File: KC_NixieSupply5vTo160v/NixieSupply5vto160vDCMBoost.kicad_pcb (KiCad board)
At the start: 2 copper layers, 38.2 x 37.9 mm, 45 parts, among them J1 Screw_Terminal_01x04, J2 CONN_01X01, J3 CONN_01X01, J4 CONN_01X01, J5 CONN_01X01, P1 USB_OTG, Q1 FDS2672CT, Q26 MMBT42, U1 UCC3803

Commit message: Updated the copyright information to Mark Smith and added www.surfncircuits.com to Boards Also added a part number and date code.    yyww (last two digits of year and ww is the work week) NixieSupply Rev2_1804 NixieSupplyMini Rev1_1804
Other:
- board text added: "Mark Smith"
- board text added: "NixieSupply Rev2_1804"
- board text added: "copyright (c) 2018"
- board text added: "www.surfncircuits.com"
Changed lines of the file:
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@@
-(kicad_pcb (version 4) (host pcbnew 4.0.7-e2-6376~58~ubuntu14.04.1)
+(kicad_pcb (version 4) (host pcbnew 4.0.7-e2-6376~60~ubuntu17.10.1)
   (general
     (links 84)
@@
     (area 17.081499 66.616595 229.894856 177.128)
     (thickness 1.6)
-    (drawings 10)
+    (drawings 14)
     (tracks 383)
     (zones 0)
@@
   (page A4)
   (layers
-    (0 F.Cu signal)
-    (31 B.Cu signal)
-    (34 B.Paste user)
-    (35 F.Paste user)
+    (0 F.Cu signal hide)
+    (31 B.Cu signal hide)
+    (34 B.Paste user hide)
+    (35 F.Paste user hide)
     (36 B.SilkS user)
-    (37 F.SilkS user)
-    (38 B.Mask user)
-    (39 F.Mask user)
-    (41 Cmts.User user)
+    (37 F.SilkS user hide)
+    (38 B.Mask user hide)
+    (39 F.Mask user hide)
+    (41 Cmts.User user hide)
     (44 Edge.Cuts user)
-    (45 Margin user)
-    (46 B.CrtYd user)
-    (47 F.CrtYd user)
-    (48 B.Fab user)
-    (49 F.Fab user)
+    (45 Margin user hide)
+    (46 B.CrtYd user hide)
+    (47 F.CrtYd user hide)
+    (48 B.Fab user hide)
+    (49 F.Fab user hide)
   )
   (setup
@@
     )
   )
+  (gr_text www.surfncircuits.com (at 152.654 105.2195) (layer B.SilkS)
+    (effects (font (size 1.5 1.5) (thickness 0.3)) (justify mirror))
+  )
+  (gr_text "copyright (c) 2018" (at 154.8765 107.569) (layer B.SilkS)
+    (effects (font (size 1.5 1.5) (thickness 0.3)) (justify mirror))
+  )
+  (gr_text "NixieSupply  Rev2_1804" (at 155.2575 98.679) (layer B.SilkS)
+    (effects (font (size 1.5 1.5) (thickness 0.3)) (justify mirror))
+  )
+  (gr_text "Mark Smith" (at 155.575 109.601) (layer B.SilkS)
+    (effects (font (size 1.5 1.5) (thickness 0.3)) (justify mirror))
+  )
   (dimension 37.858719 (width 0.3) (layer F.Fab)

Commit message: Added OSHW_LOGO and the copyright symbol to both Files.    Also updated the gerber files and finished the Mini layout solution.
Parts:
- added G***: OSHW_logo_silkscreen-front_5mm, OSHW_logo_silkscreen-front_5mm, B.Cu at (155.8, 102.2)
- added G***: LOGO, LOGO, B.Cu at (162.6, 108.5)
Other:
- board text added: "Mark Smith 2018"
- board text removed: "Mark Smith"
- board text removed: "copyright (c) 2018"

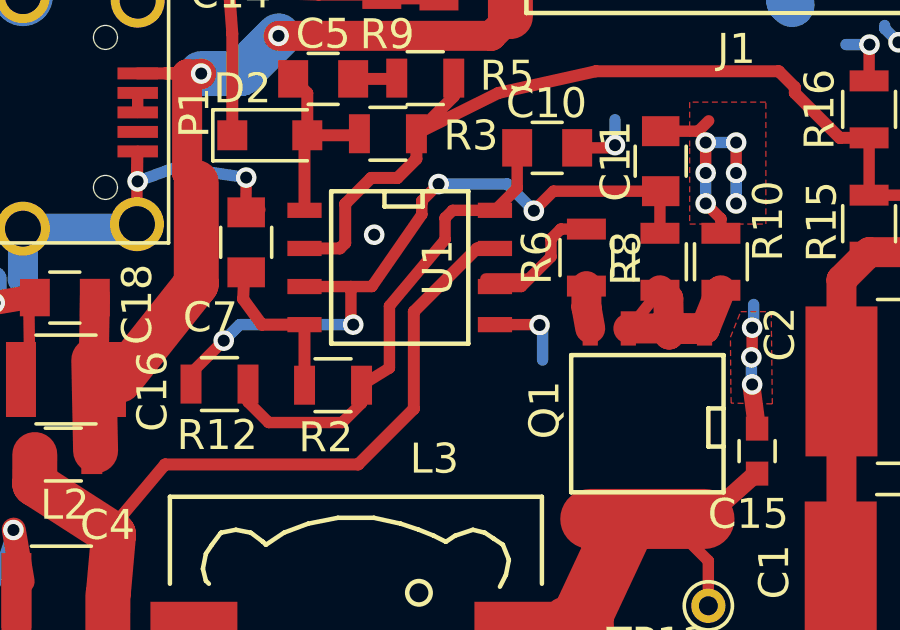
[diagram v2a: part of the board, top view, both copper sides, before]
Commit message: Updated the gerber files to include a ground pad for R10 to reduce resistance.  Also updated the net classes for the blog entry.
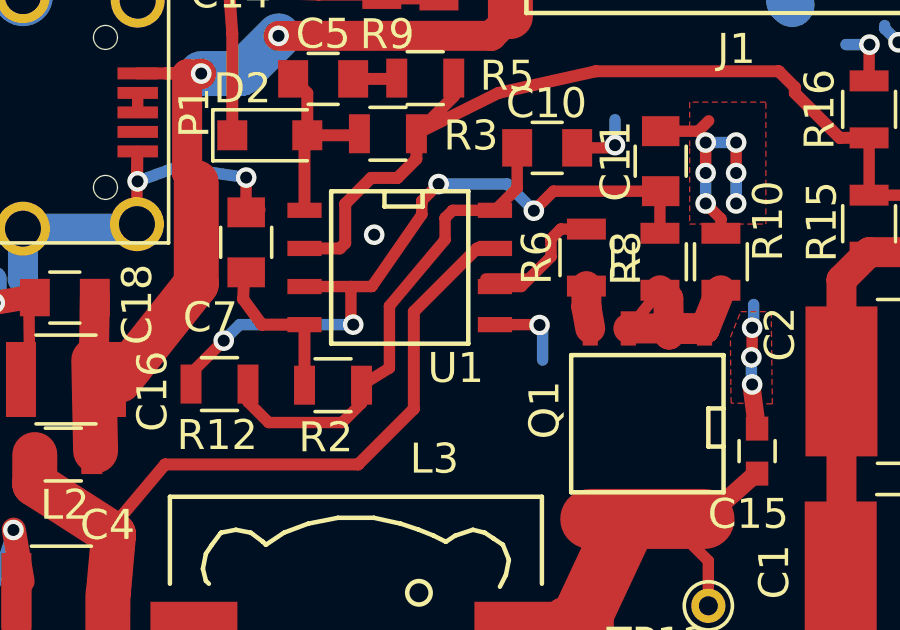
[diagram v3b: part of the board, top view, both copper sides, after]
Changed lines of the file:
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@@
-(kicad_pcb (version 4) (host pcbnew 4.0.7-e2-6376~60~ubuntu17.10.1)
+(kicad_pcb (version 4) (host pcbnew 4.0.7-e2-6376~58~ubuntu14.04.1)
   (general
     (links 84)
@@
     (tags "CMS SOJ")
     (attr smd)
-    (fp_text reference U1 (at 0 -1.27 270) (layer F.SilkS)
-      (effects (font (size 1 1) (thickness 0.15)))
-    )
+    (fp_text reference U1 (at 3.3528 -1.8669 540) (layer F.SilkS)
+      (effects (font (size 1 1) (thickness 0.15)))
+    )

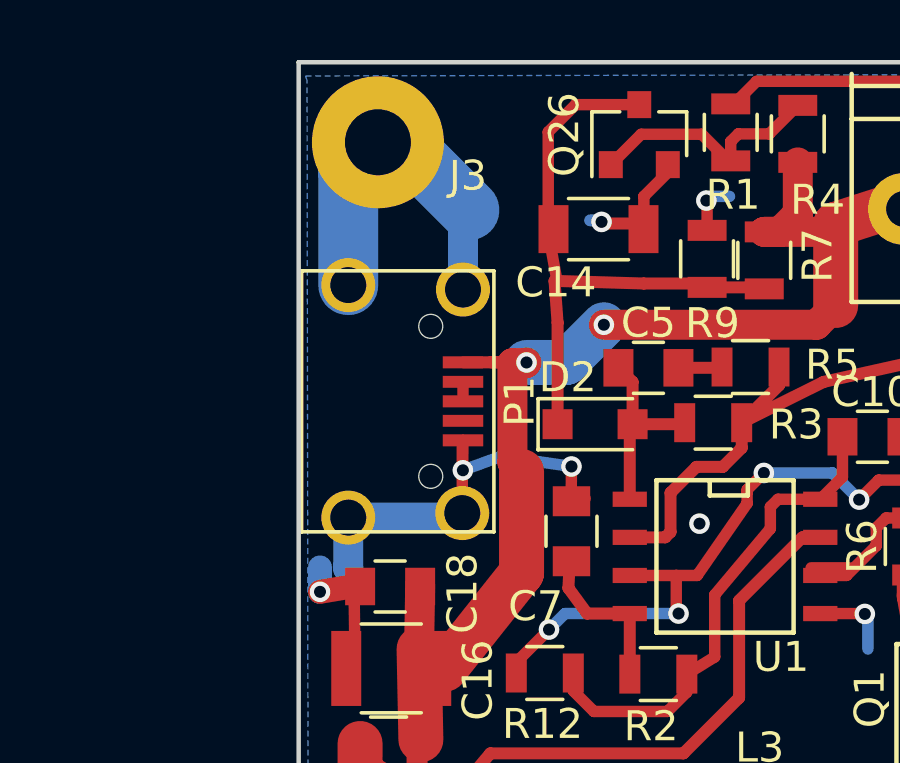
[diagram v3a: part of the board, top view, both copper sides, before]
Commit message: New Rev 3 for the Original Nixie Power Supply 1. Corner Mounting Holes are now Solid.  Per the tip by comment reader 2. The original supply has a better ground connection for the USB input,     But the USB connector shield is still grounded. 2.5. The D+ and D- USB inputs are unshorted. 3. The revision was updated to Rev 3 for the Original Supply and Rev 2 for the Mini Supply 4. New Gerbers were created and zip files
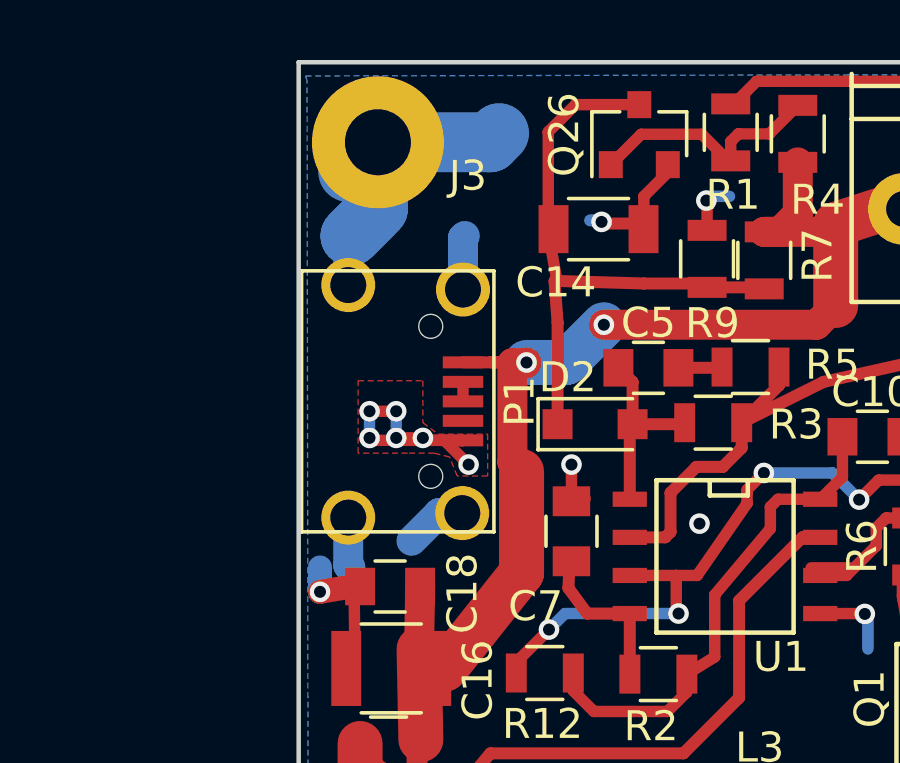
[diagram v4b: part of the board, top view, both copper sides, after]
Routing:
- net GND: track 145.0 -> 148.4 mm, vias 33 -> 38
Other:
- board text added: "NixieSupply Rev3_1810"
- board text removed: "NixieSupply Rev2_1804"
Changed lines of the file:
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@@
-(kicad_pcb (version 4) (host pcbnew 4.0.7-e2-6376~58~ubuntu14.04.1)
+(kicad_pcb (version 4) (host pcbnew 4.0.6+dfsg1-1)
   (general
     (links 84)
     (no_connects 0)
-    (area 135.992799 73.127799 174.369801 111.187301)
+    (area 17.081499 66.616595 229.894856 177.128)
     (thickness 1.6)
     (drawings 13)
-    (tracks 383)
+    (tracks 401)
     (zones 0)
     (modules 47)
@@
     (user_trace_width 2)
     (trace_clearance 0.254)
-    (zone_clearance 0.2)
+    (zone_clearance 0.508)
     (zone_45_only no)
     (trace_min 0.1524)
@@
     (mod_text_size 1 1)
     (mod_text_width 0.15)
-    (pad_size 1.143 1.143)
-    (pad_drill 0.635)
+    (pad_size 4.4 4.4)
+    (pad_drill 2.2)
     (pad_to_mask_clearance 0.0508)
     (aux_axis_origin 136.0932 73.1774)
@@
     (fp_circle (center 0 0) (end 2.45 0) (layer F.CrtYd) (width 0.05))
     (pad 1 thru_hole circle (at 0 0) (size 4.4 4.4) (drill 2.2) (layers *.Cu *.Mask)
-      (net 1 GND))
+      (net 1 GND) (zone_connect 2))
   )
   (module Mounting_Holes:MountingHole_2.2mm_M2_Pad (layer F.Cu)
@@
     (fp_circle (center 0 0) (end 2.45 0) (layer F.CrtYd) (width 0.05))
     (pad 1 thru_hole circle (at 0 0) (size 4.4 4.4) (drill 2.2) (layers *.Cu *.Mask)
-      (net 1 GND))
+      (net 1 GND) (zone_connect 2))
   )
   (module Capacitors_SMD:C_0805 (layer F.Cu)
@@
     (effects (font (size 1.5 1.5) (thickness 0.3)) (justify mirror))
   )
-  (gr_text "NixieSupply  Rev2_1804" (at 155.2575 98.679) (layer B.SilkS)
+  (gr_text "NixieSupply  Rev3_1810" (at 155.2575 98.679) (layer B.SilkS)
     (effects (font (size 1.5 1.5) (thickness 0.3)) (justify mirror))
   )
@@
   (via (at 149.4282 88.5825) (size 0.6858) (drill 0.4) (layers F.Cu B.Cu) (net 0))
   (segment (start 17.526 143.2633) (end 17.526 142.9893) (width 0.381) (layer F.Cu) (net 0))
+  (segment (start 140.7502 88.2308) (end 139.827 89.154) (width 1) (layer B.Cu) (net 1))
+  (segment (start 141.5203 88.2308) (end 140.7502 88.2308) (width 1) (layer B.Cu) (net 1))
+  (segment (start 137.7203 89.9683) (end 137.795 90.043) (width 1) (layer B.Cu) (net 1))
+  (segment (start 137.7203 88.3808) (end 137.7203 89.9683) (width 1) (layer B.Cu) (net 1))
+  (segment (start 141.5453 79.0537) (end 141.605 78.994) (width 1) (layer B.Cu) (net 1))
+  (segment (start 141.5453 80.7808) (end 141.5453 79.0537) (width 1) (layer B.Cu) (net 1))
+  (segment (start 137.795 78.867) (end 137.795 78.994) (width 1) (layer B.Cu) (net 1))
+  (segment (start 137.795 78.994) (end 137.795 78.867) (width 1) (layer B.Cu) (net 1))
+  (segment (start 137.7203 79.0687) (end 137.795 78.994) (width 1) (layer B.Cu) (net 1))
+  (segment (start 137.7203 80.6308) (end 137.7203 79.0687) (width 1) (layer B.Cu) (net 1))
+  (segment (start 137.795 78.994) (end 138.557 78.232) (width 2) (layer B.Cu) (net 1))
+  (segment (start 140.208 85.725) (end 139.319 85.725) (width 0.381) (layer F.Cu) (net 1))
+  (segment (start 138.5108 85.8058) (end 140.9238 85.8058) (width 0.381) (layer F.Cu) (net 1))
+  (segment (start 138.43 85.725) (end 138.5108 85.8058) (width 0.381) (layer F.Cu) (net 1))
+  (via (at 138.43 85.725) (size 0.6858) (drill 0.4) (layers F.Cu B.Cu) (net 1))
+  (segment (start 138.43 84.836) (end 138.43 85.725) (width 0.381) (layer B.Cu) (net 1))
+  (via (at 138.43 84.836) (size 0.6858) (drill 0.4) (layers F.Cu B.Cu) (net 1))
+  (segment (start 139.319 84.836) (end 138.43 84.836) (width 0.381) (layer F.Cu) (net 1))
+  (via (at 139.319 84.836) (size 0.6858) (drill 0.4) (layers F.Cu B.Cu) (net 1))
+  (segment (start 139.319 85.725) (end 139.319 84.836) (width 0.381) (layer B.Cu) (net 1))
+  (via (at 139.319 85.725) (size 0.6858) (drill 0.4) (layers F.Cu B.Cu) (net 1))
+  (segment (start 140.9238 85.8058) (end 141.732 86.614) (width 0.381) (layer F.Cu) (net 1))
+  (via (at 141.732 86.614) (size 0.6858) (drill 0.4) (layers F.Cu B.Cu) (net 1))
+  (segment (start 145.161 87.8365) (end 145.161 86.614) (width 0.381) (layer F.Cu) (net 1))
+  (via (at 145.161 86.614) (size 0.6858) (drill 0.4) (layers F.Cu B.Cu) (net 1))
+  (segment (start 141.5453 85.8058) (end 140.2888 85.8058) (width 0.381) (layer F.Cu) (net 1))
+  (segment (start 140.208 85.725) (end 139.573 85.725) (width 0.381) (layer B.Cu) (net 1))
+  (via (at 140.208 85.725) (size 0.6858) (drill 0.4) (layers F.Cu B.Cu) (net 1))
+  (segment (start 140.2888 85.8058) (end 140.208 85.725) (width 0.381) (layer F.Cu) (net 1))
+  (segment (start 138.7094 75.8698) (end 138.7094 78.0796) (width 2) (layer B.Cu) (net 1))
+  (segment (start 138.7094 78.0796) (end 137.795 78.994) (width 2) (layer B.Cu) (net 1))
+  (segment (start 138.7094 75.8698) (end 142.4432 75.8698) (width 2) (layer B.Cu) (net 1))
+  (segment (start 142.4432 75.8698) (end 142.748 75.565) (width 2) (layer B.Cu) (net 1))
   (segment (start 137.5029 100.1649) (end 137.5015 103.6828) (width 1) (layer F.Cu) (net 1))
   (segment (start 162.1917 95.0461) (end 162.0012 93.599) (width 0.6) (layer F.Cu) (net 1) (status 10))
@@
   (segment (start 136.779 90.8558) (end 136.779 90.043) (width 0.8) (layer B.Cu) (net 1))
   (via (at 136.779 90.8558) (size 0.6858) (drill 0.4) (layers F.Cu B.Cu) (net 1))
-  (segment (start 137.7203 88.3808) (end 137.7203 90.0415) (width 1) (layer B.Cu) (net 1))
-  (segment (start 137.7203 90.0415) (end 137.7061 90.0557) (width 1) (layer B.Cu) (net 1))
-  (segment (start 137.7203 88.3808) (end 141.3703 88.3808) (width 1) (layer B.Cu) (net 1))
-  (segment (start 141.3703 88.3808) (end 141.5203 88.2308) (width 1) (layer B.Cu) (net 1))
-  (segment (start 141.5453 80.7808) (end 141.5453 78.3425) (width 1) (layer B.Cu) (net 1))
-  (segment (start 141.7574 78.1304) (end 139.4968 75.8698) (width 2) (layer B.Cu) (net 1))
-  (segment (start 141.5453 78.3425) (end 141.7574 78.1304) (width 0.8) (layer B.Cu) (net 1))
-  (segment (start 137.7203 80.6308) (end 137.7203 76.8589) (width 2) (layer B.Cu) (net 1))
   (segment (start 137.7203 76.8589) (end 138.7094 75.8698) (width 2) (layer B.Cu) (net 1))
   (segment (start 138.7094 75.8698) (end 139.4968 75.8698) (width 2) (layer B.Cu) (net 1))
@@
   (via (at 157.4546 85.598) (size 0.6858) (drill 0.4) (layers F.Cu B.Cu) (net 1))
   (segment (start 157.3657 85.6869) (end 157.4546 85.598) (width 0.381) (layer F.Cu) (net 1))
-  (segment (start 137.8618 88.5223) (end 137.7203 88.3808) (width 0.381) (layer F.Cu) (net 1))
   (segment (start 137.9507 93.4339) (end 137.9126 90.6653) (width 0.381) (layer F.Cu) (net 1) (status 20))
   (segment (start 137.7108 100.1395) (end 137.414 98.4123) (width 0.8) (layer F.Cu) (net 1) (status 10))
@@
   (segment (start 146.2184 78.5782) (end 146.1643 78.5241) (width 0.4) (layer F.Cu) (net 1))
   (segment (start 145.6182 87.7476) (end 145.1516 87.7476) (width 0.381) (layer F.Cu) (net 1) (status 30))
-  (segment (start 145.1516 87.7476) (end 145.161 86.6775) (width 0.381) (layer F.Cu) (net 1) (status 10))
-  (via (at 145.161 86.6775) (size 0.6858) (drill 0.4) (layers F.Cu B.Cu) (net 1))
-  (segment (start 145.161 86.6775) (end 142.8242 86.3346) (width 0.381) (layer B.Cu) (net 1))
-  (segment (start 142.8242 86.3346) (end 141.5415 86.8045) (width 0.381) (layer B.Cu) (net 1))
-  (via (at 141.5415 86.8045) (size 0.6858) (drill 0.4) (layers F.Cu B.Cu) (net 1))
-  (segment (start 141.5415 86.8045) (end 141.5334 86.7964) (width 0.381) (layer F.Cu) (net 1))
-  (segment (start 141.5334 86.7964) (end 141.5453 85.8058) (width 0.381) (layer F.Cu) (net 1))
-  (segment (start 141.5203 88.2308) (end 141.5203 85.8308) (width 0.381) (layer F.Cu) (net 1))
   (segment (start 141.5203 85.8308) (end 141.5453 85.8058) (width 0.381) (layer F.Cu) (net 1))
-  (segment (start 137.8703 88.2308) (end 137.7203 88.3808) (width 0.381) (layer F.Cu) (net 1))
   (segment (start 153.4541 91.5797) (end 154.9273 91.5797) (width 0.381) (layer F.Cu) (net 1))
   (segment (start 155.0416 91.694) (end 155.0416 92.7608) (width 0.381) (layer B.Cu) (net 1))
@@
   (segment (start 149.6822 77.8383) (end 149.6568 77.8129) (width 0.381) (layer F.Cu) (net 1))
   (segment (start 148.4978 76.4896) (end 148.3716 76.6158) (width 0.381) (layer F.Cu) (net 1))
+  (segment (start 141.3703 88.3808) (end 141.5203 88.2308) (width 1) (layer B.Cu) (net 1))
+  (segment (start 137.8618 88.5223) (end 137.7203 88.3808) (width 0.381) (layer F.Cu) (net 1))
+  (segment (start 137.8703 88.2308) (end 137.7203 88.3808) (width 0.381) (layer F.Cu) (net 1))
   (segment (start 147.1041 87.7697) (end 147.1041 85.3621) (width 0.4) (layer F.Cu) (net 2))
   (segment (start 147.1041 85.3621) (end 147.1984 85.2678) (width 0.4) (layer F.Cu) (net 2))
@@
       )
     )
+  )
+  (zone (net 1) (net_name GND) (layer F.Cu) (hatch edge 0.508)
+    (connect_pads (clearance 0.508))
+    (min_thickness 0.254)
+    (fill yes (arc_segments 16) (thermal_gap 0.508) (thermal_bridge_width 0.508))
+    (polygon
+      (pts
+        (xy 142.367 85.598) (xy 142.367 86.995) (xy 141.351 86.995) (xy 141.097 86.36) (xy 140.589 86.233)
+        (xy 139.7 86.233) (xy 138.049 86.233) (xy 138.049 83.82) (xy 140.208 83.82) (xy 140.208 85.217)
+        (xy 140.716 85.598)
+      )
+    )
